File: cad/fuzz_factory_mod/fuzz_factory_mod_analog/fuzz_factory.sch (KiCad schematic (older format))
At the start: 26 parts, among them Q901 Q_NJFET_DSG, Q902 DMMT3904W, Q903 DMMT3906W, Q904 DMMT3906W

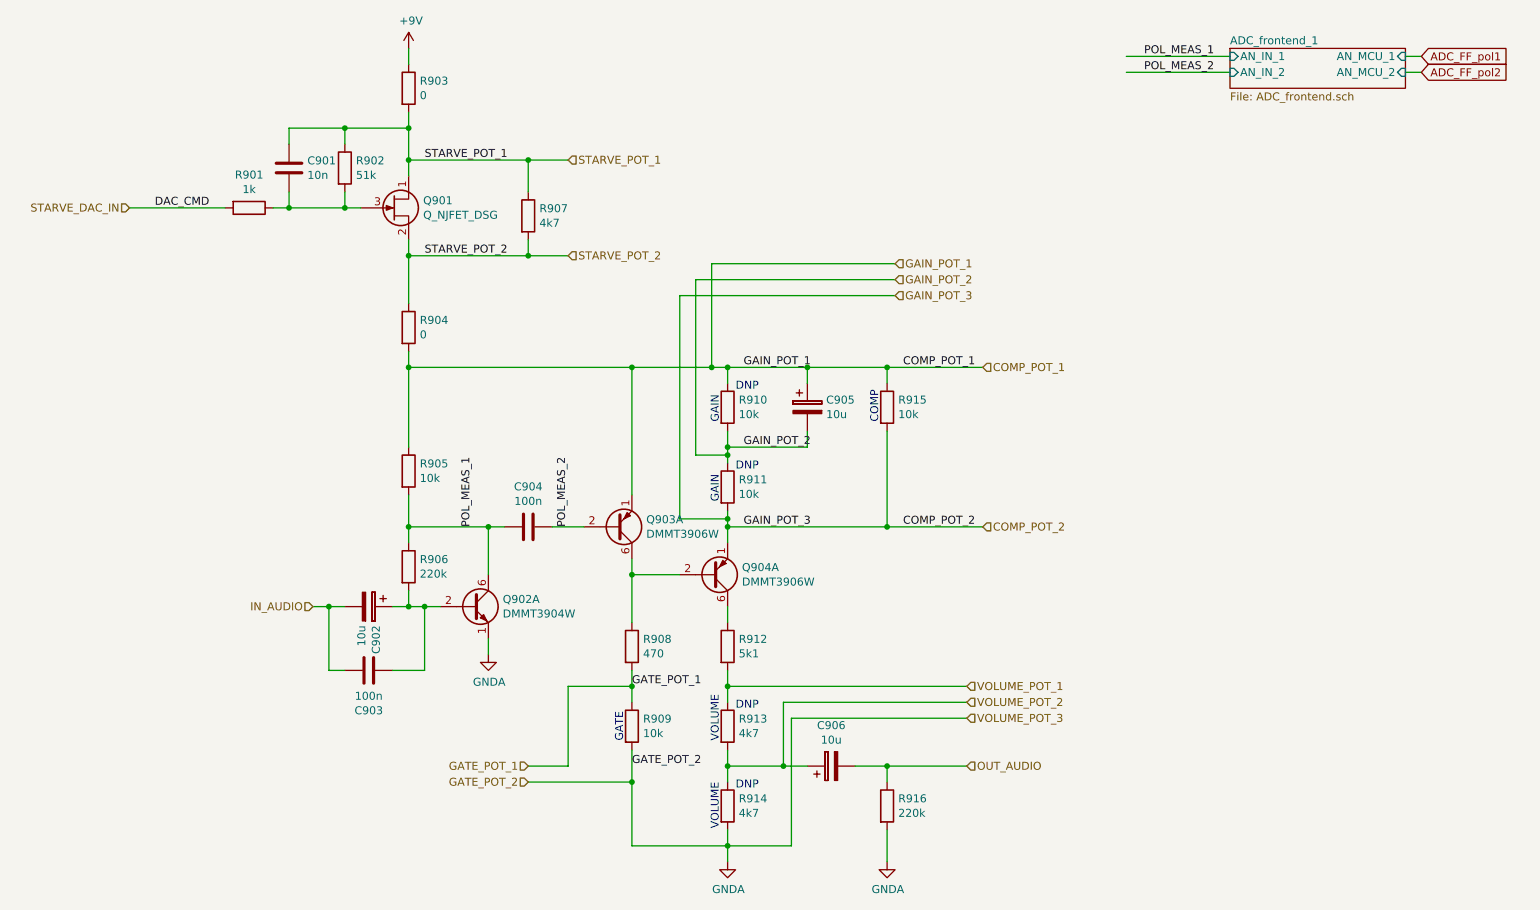
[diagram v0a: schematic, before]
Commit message: Changes architecture.
Corrections on schematic.
Continued Layout placement.
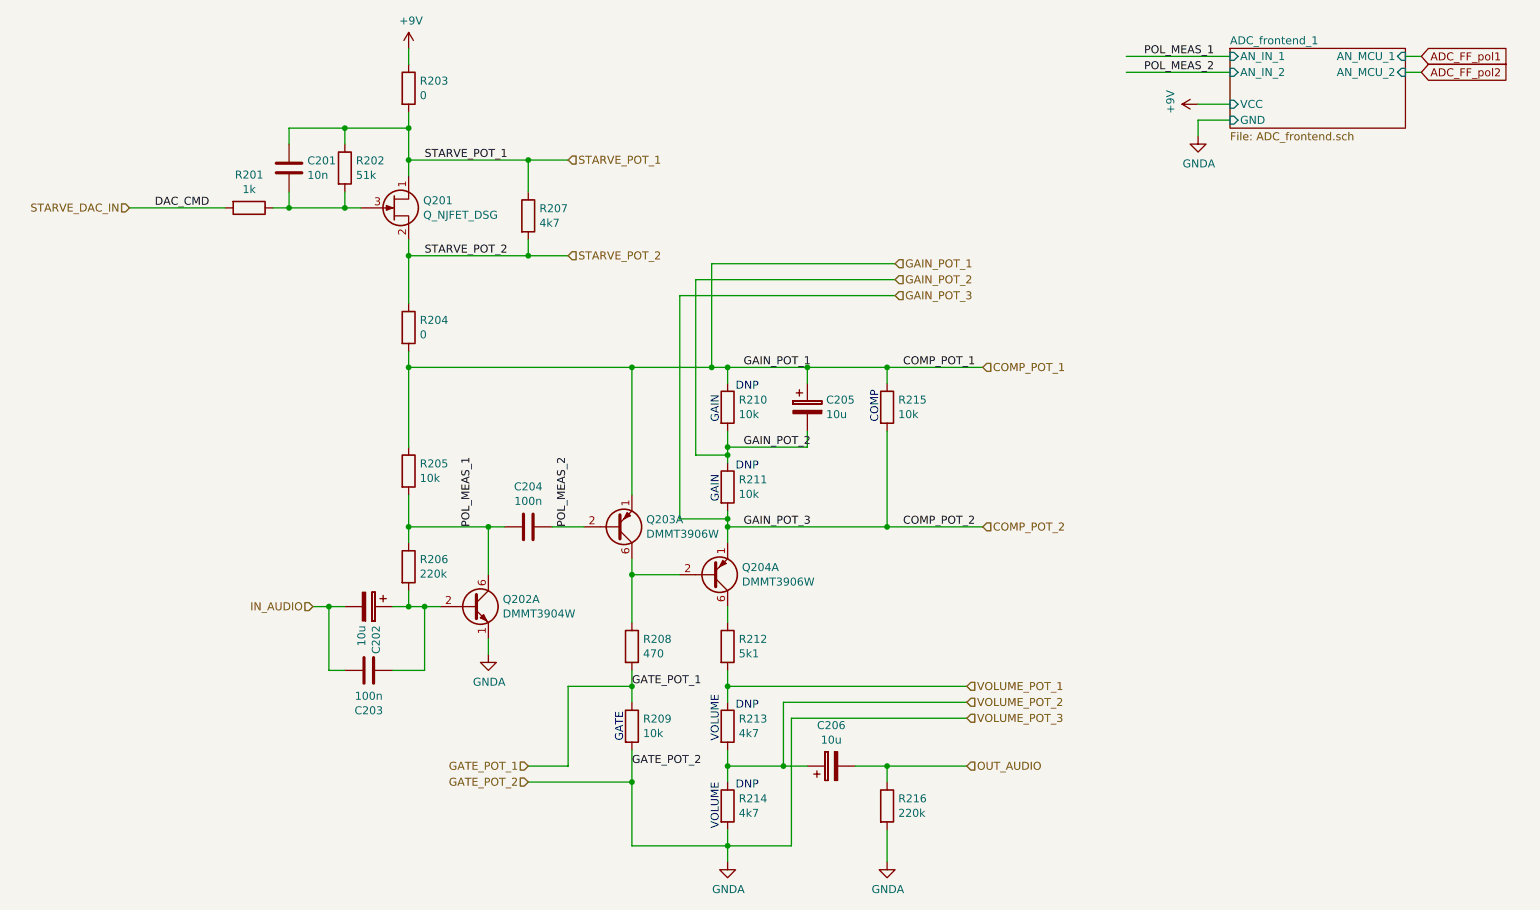
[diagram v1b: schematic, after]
